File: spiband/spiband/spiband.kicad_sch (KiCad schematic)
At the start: 25 parts, among them J1 RJ45_Shielded, J5 Conn_01x02, U1 MAX3485, U11 LM1086CT-3.3, U2 MAX3485, U3 MAX3485, U4 MAX3232, U5 74HC04, U6 TLV70018_SOT353, U7 74HC153

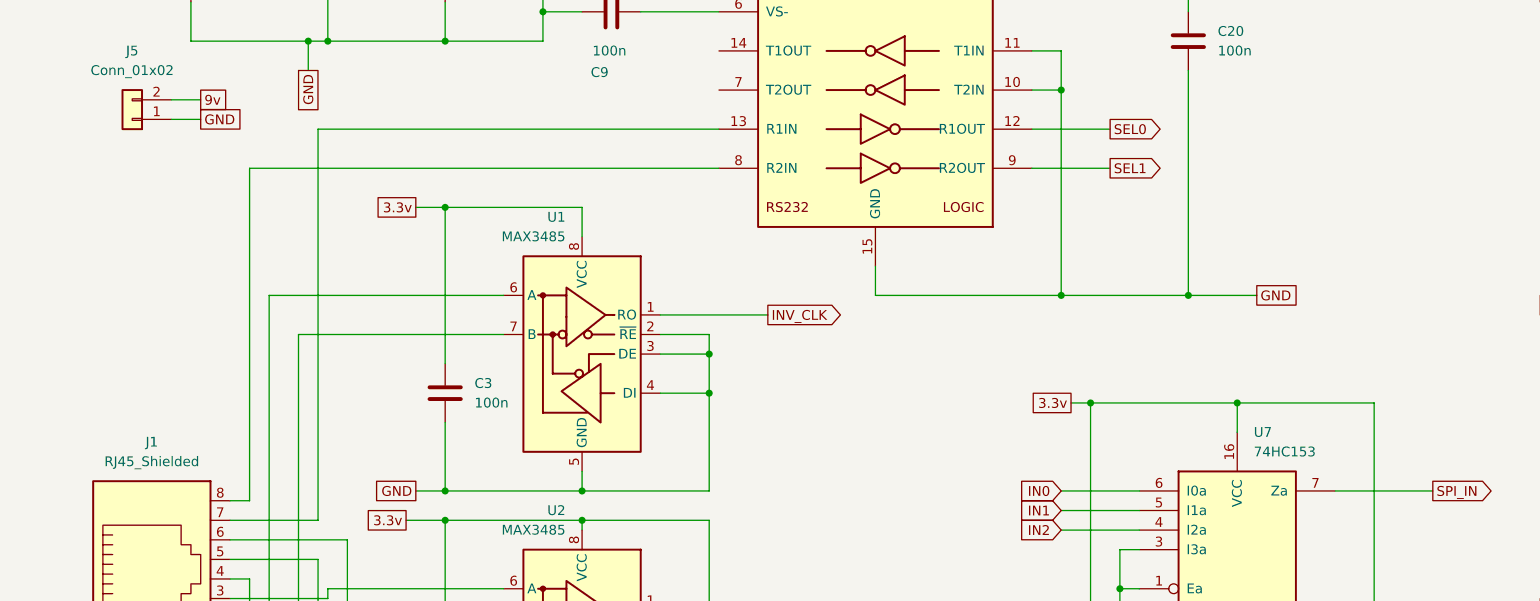
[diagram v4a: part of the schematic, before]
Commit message: Reworked ADCIO project to use DAC IO.
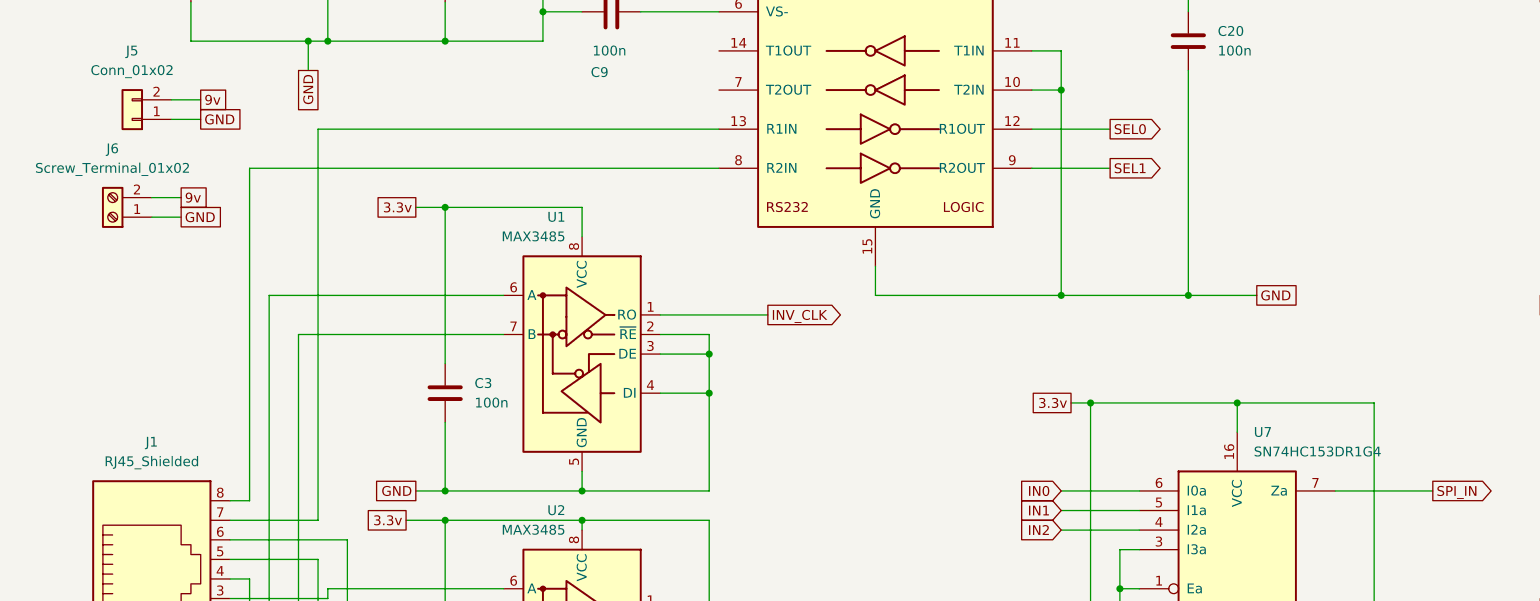
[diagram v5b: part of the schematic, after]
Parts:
- added J6: Screw_Terminal_01x02, TerminalBlock_Phoenix:TerminalBlock_Phoenix_MKDS-1,5-2_1x02_P5.00mm_Horizontal, symbol Connector:Screw_Terminal_01x02
- U7: value 74HC153 -> SN74HC153DR1G4
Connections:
- net 9v: now also J6.2 (Pin_2)
- net GND: now also J6.1 (Pin_1)
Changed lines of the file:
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@@
 	(wire
 		(pts
+			(xy 22.86 69.85) (xy 26.67 69.85)
+		)
+		(stroke
+			(width 0)
+			(type default)
+		)
+	)
+	(wire
+		(pts
 			(xy 271.78 69.85) (xy 274.32 69.85)
 		)
@@
 	(wire
 		(pts
+			(xy 22.86 72.39) (xy 26.67 72.39)
+		)
+		(stroke
+			(width 0)
+			(type default)
+		)
+	)
+	(wire
+		(pts
 			(xy 68.58 120.65) (xy 45.72 120.65)
 		)
@@
 	(global_label "GND"
 		(shape passive)
+		(at 26.67 72.39 0)
+		(fields_autoplaced yes)
+		(effects
+			(font
+				(size 1.27 1.27)
+			)
+			(justify left)
+		)
+		(property "Intersheetrefs" "${INTERSHEET_REFS}"
+			(at 32.4144 72.39 0)
+			(hide yes)
+			(show_name no)
+			(do_not_autoplace no)
+			(effects
+				(font
+					(size 1.27 1.27)
+				)
+				(justify left)
+			)
+		)
+	)
+	(global_label "GND"
+		(shape passive)
 		(at 208.28 43.18 180)
 		(fields_autoplaced yes)
@@
 		)
 	)
+	(global_label "9v"
+		(shape passive)
+		(at 26.67 69.85 0)
+		(fields_autoplaced yes)
+		(effects
+			(font
+				(size 1.27 1.27)
+			)
+			(justify left)
+		)
+		(property "Intersheetrefs" "${INTERSHEET_REFS}"
+			(at 30.721 69.85 0)
+			(hide yes)
+			(show_name no)
+			(do_not_autoplace no)
+			(effects
+				(font
+					(size 1.27 1.27)
+				)
+				(justify left)
+			)
+		)
+	)
 	(global_label "IN0"
 		(shape input)
@@
 	)
 	(symbol
+		(lib_id "Connector:Screw_Terminal_01x02")
+		(at 17.78 72.39 180)
+		(unit 1)
+		(body_style 1)
+		(exclude_from_sim no)
+		(in_bom yes)
+		(on_board yes)
+		(in_pos_files yes)
+		(dnp no)
+		(fields_autoplaced yes)
+		(property "Reference" "J6"
+			(at 17.78 63.5 0)
+			(show_name no)
+			(do_not_autoplace no)
+			(effects
+				(font
+					(size 1.27 1.27)
+				)
+			)
+		)
+		(property "Value" "Screw_Terminal_01x02"
+			(at 17.78 66.04 0)
+			(show_name no)
+			(do_not_autoplace no)
+			(effects
+				(font
+					(size 1.27 1.27)
+				)
+			)
+		)
+		(property "Footprint" "TerminalBlock_Phoenix:TerminalBlock_Phoenix_MKDS-1,5-2_1x02_P5.00mm_Horizontal"
+			(at 17.78 72.39 0)
+			(hide yes)
+			(show_name no)
+			(do_not_autoplace no)
+			(effects
+				(font
+					(size 1.27 1.27)
+				)
+			)
+		)
+		(property "Datasheet" ""
+			(at 17.78 72.39 0)
+			(hide yes)
+			(show_name no)
+			(do_not_autoplace no)
+			(effects
+				(font
+					(size 1.27 1.27)
+				)
+			)
+		)
+		(property "Description" "Generic screw terminal, single row, 01x02, script generated (kicad-library-utils/schlib/autogen/connector/)"
+			(at 17.78 72.39 0)
+			(hide yes)
+			(show_name no)
+			(do_not_autoplace no)
+			(effects
+				(font
+					(size 1.27 1.27)
+				)
+			)
+		)
+		(pin "1"
+		)
+		(pin "2"
+		)
+		(instances
+			(project "spiband"
+				(path "/8368e55c-e309-4bdd-b721-ce7a0ff80dac"
+					(reference "J6")
+					(unit 1)
+				)
+			)
+		)
+	)
+	(symbol
 		(lib_id "Interface_UART:MAX3232")
 		(at 116.84 48.26 0)
@@
 			)
 		)
-		(property "Value" "74HC153"
+		(property "Value" "SN74HC153DR1G4"
 			(at 165.9733 102.87 0)
 			(show_name no)

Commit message: Updated footprints for RJ45 and balun height.
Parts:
- J1: footprint Connector_RJ:RJ45_Amphenol_RJHSE5380 -> custom:RJ45
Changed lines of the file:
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@@
 			)
 		)
-		(property "Footprint" "Connector_RJ:RJ45_Amphenol_RJHSE5380"
+		(property "Footprint" "custom:RJ45"
 			(at 22.86 118.745 90)
 			(hide yes)
